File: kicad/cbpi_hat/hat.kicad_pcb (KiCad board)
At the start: 2 copper layers, 65 x 56 mm, 38 parts, among them J1 GPIO, J2 Screw_Terminal_01x02, Q1 HY15P03C2, Q2 DMG2305UX, Q3 DMMT5401-7-F, U1 CAT24C256, U2 EUP3453WIR1

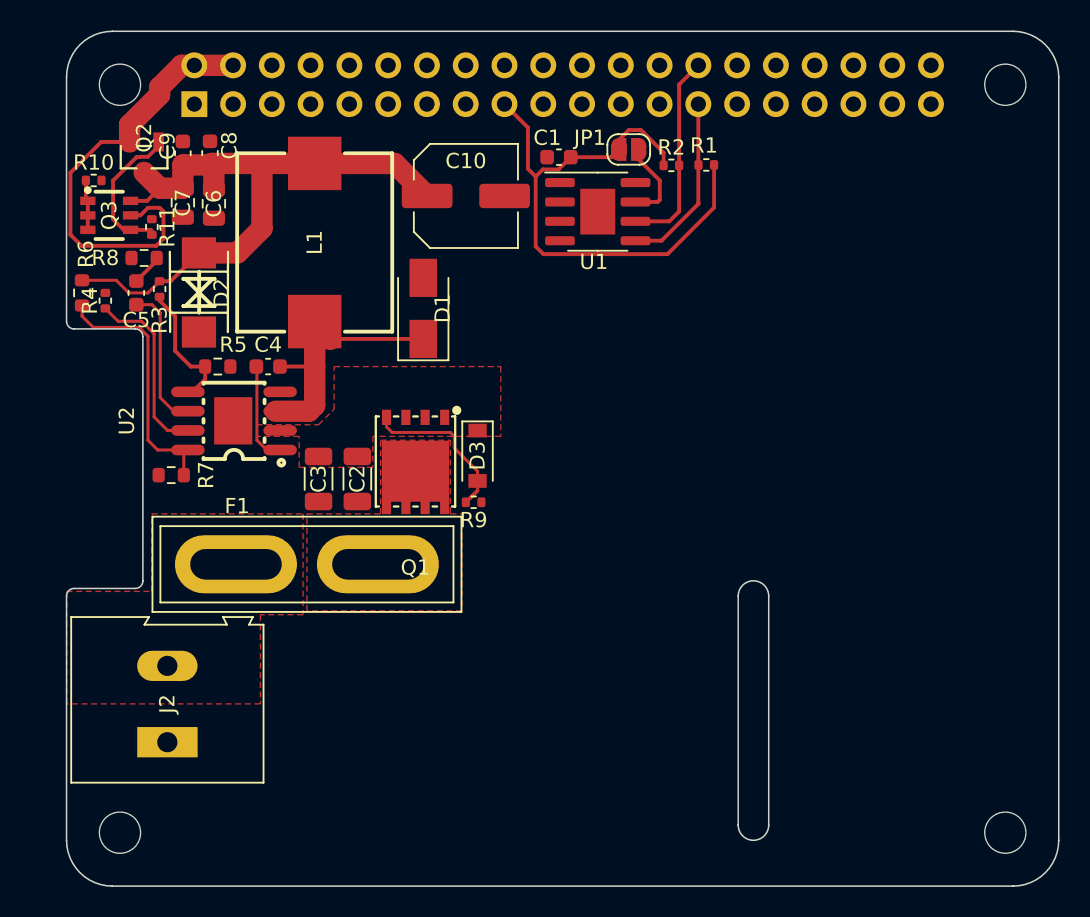
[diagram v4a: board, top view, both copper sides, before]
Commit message: Added RTC to board
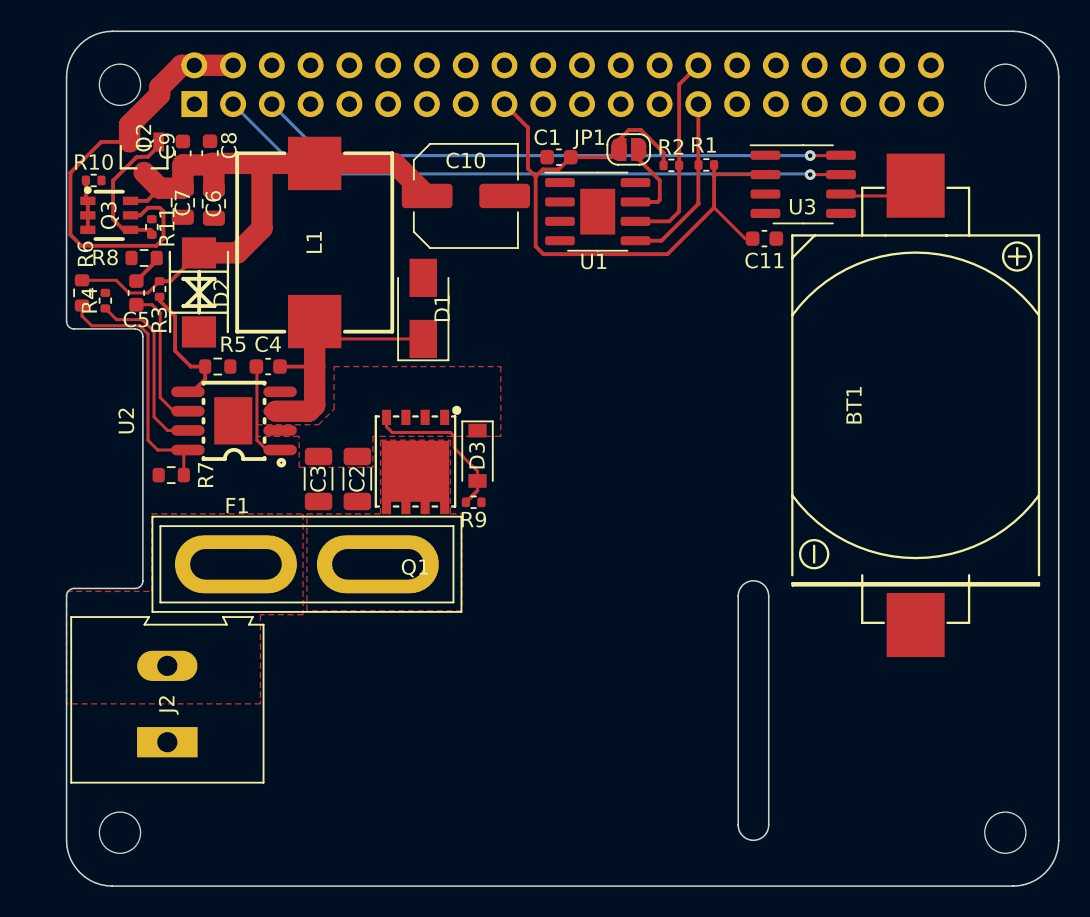
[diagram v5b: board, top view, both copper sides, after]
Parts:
- added BT1: Battery_Cell, cr2032-bs-6-1:BAT-TH_CR2032-BS-6-1, F.Cu at (155.6, 68.5)
- added C11: 100nF, Capacitor_SMD:C_0603_1608Metric, F.Cu at (145.7, 57.6)
- added U3: DS3231MZ, Package_SO:SOIC-8_3.9x4.9mm_P1.27mm, F.Cu at (148.3, 54.0)
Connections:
- J1 pad 3: /GPIO[2]/SDA1 -> I2C_SDA
- J1 pad 5: /GPIO[3]/SCL1 -> I2C_SCL
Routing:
- net I2C_SDA: track 0.00 -> 41.7 mm, vias 0 -> 1
- net I2C_SCL: track 0.00 -> 38.7 mm, vias 0 -> 1
- net +3.3V: track 38.6 -> 45.4 mm
- net Net-(BT1-Pad1): track 0.00 -> 5.47 mm

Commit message: Added power and warning LED. This should address #13 and fix it
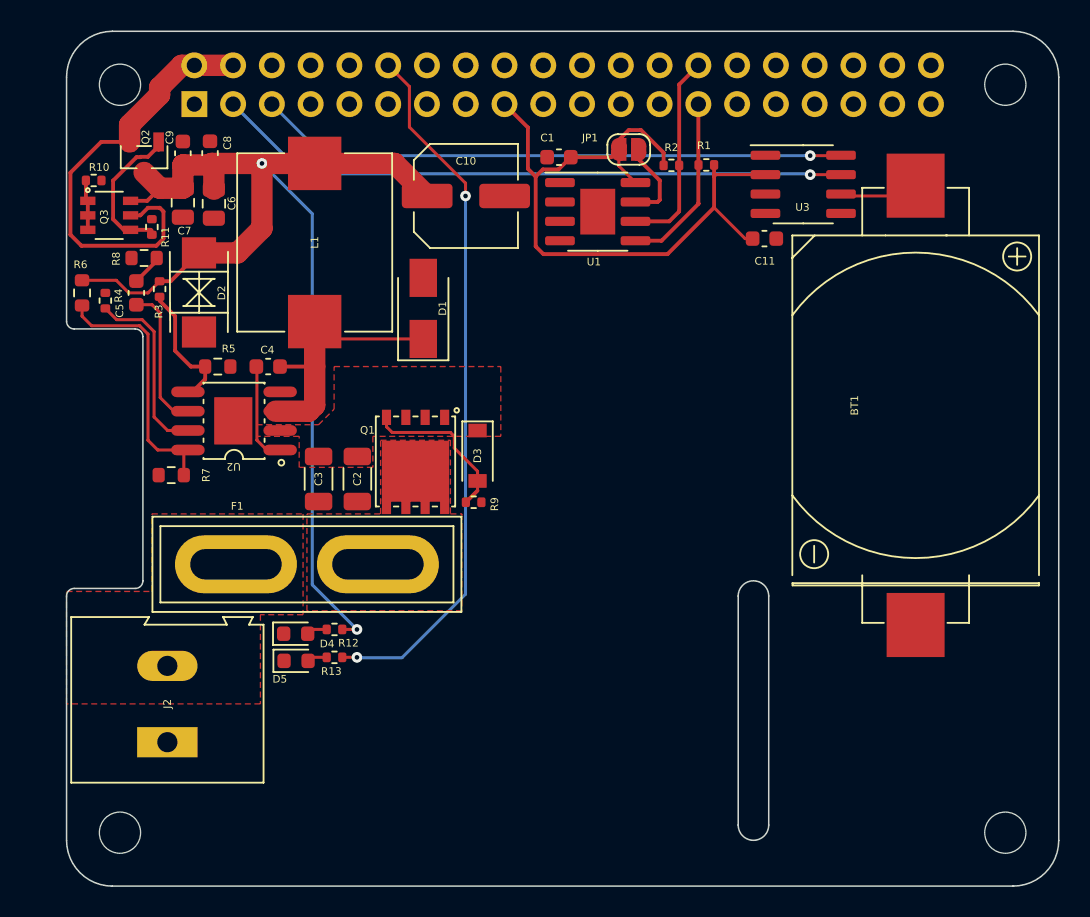
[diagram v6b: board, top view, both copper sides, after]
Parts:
- added D4: LED, LED_SMD:LED_0603_1608Metric, F.Cu at (115.0, 83.5)
- added D5: LED, LED_SMD:LED_0603_1608Metric, F.Cu at (115.0, 85.2)
- added R12: 220, Resistor_SMD:R_0402_1005Metric, F.Cu at (117.6, 83.2)
- added R13: 91, Resistor_SMD:R_0402_1005Metric, F.Cu at (117.6, 85.0)
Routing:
- net /GPIO[18]/PCM.CLK: track 0.00 -> 46.6 mm, vias 0 -> 2
- net +5V: track 43.8 -> 77.9 mm, vias 0 -> 2
- net +3.3V: track 45.4 -> 48.0 mm
- net Net-(D4-Pad2): track 0.00 -> 1.36 mm
- net Net-(D5-Pad2): track 0.00 -> 1.31 mm

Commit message: Replaced CR2032 holder with the old more space saving one and fixed all DRC errors and warnings except for unconnected GND
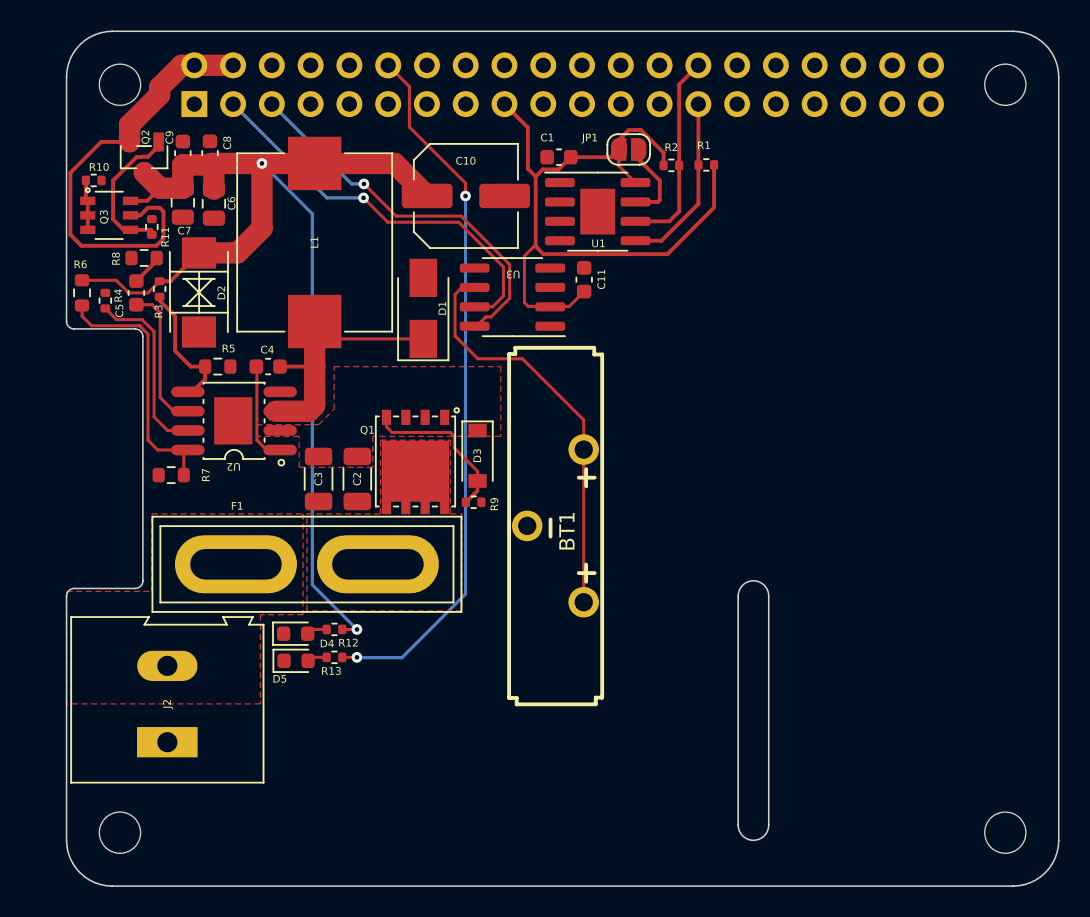
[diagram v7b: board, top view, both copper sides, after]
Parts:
- BT1: footprint cr2032-bs-6-1:BAT-TH_CR2032-BS-6-1 -> cr2032-bs-5-1:BAT-TH_CR2032-BS-5-1
- moved BT1 24.9 mm to (132.0, 76.4)
- moved U3 20.4 mm to (129.2, 61.4), turned to 180 degrees
- moved C11 12.1 mm to (133.9, 60.3), turned to 90 degrees
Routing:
- net Net-(BT1-Pad1): track 5.47 -> 27.0 mm
- net I2C_SDA: track 41.7 -> 26.1 mm
- net I2C_SCL: track 38.7 -> 25.0 mm
- net Net-(C4-Pad1): track 7.23 -> 5.75 mm
- net +3.3V: track 48.0 -> 48.7 mm
- net Net-(R3-Pad1): track 8.96 -> 8.36 mm
